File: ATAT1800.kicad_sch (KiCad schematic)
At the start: 336 parts, among them J1 USB_C_Receptacle_USB2.0, SW1 MX_SW_solder, SW10 MX_SW_solder, SW100 MX_SW_solder, SW101 MX_SW_solder, SW102 SW_SPDT, SW11 MX_SW_solder, SW12 MX_SW_solder, SW13 MX_SW_solder, SW14 MX_SW_solder, SW15 MX_SW_solder, SW16 MX_SW_solder, SW17 MX_SW_solder, SW18 MX_SW_solder, SW19 MX_SW_solder, SW2 MX_SW_solder, SW20 MX_SW_solder, SW21 MX_SW_solder, SW22 MX_SW_solder, SW23 MX_SW_solder, SW24 MX_SW_solder, SW25 MX_SW_solder, SW26 MX_SW_solder, SW27 MX_SW_solder, SW28 MX_SW_solder, SW29 MX_SW_solder, SW3 MX_SW_solder, SW30 MX_SW_solder, SW31 MX_SW_solder, SW32 MX_SW_solder, SW33 MX_SW_solder, SW34 MX_SW_solder, SW35 MX_SW_solder, SW36 MX_SW_solder, SW37 MX_SW_solder, SW38 MX_SW_solder, SW39 MX_SW_solder, SW4 MX_SW_solder, SW40 MX_SW_solder, SW41 MX_SW_solder, SW42 MX_SW_solder, SW43 MX_SW_solder, SW44 MX_SW_solder, SW45 MX_SW_solder, SW46 MX_SW_solder, SW47 MX_SW_solder, SW48 MX_SW_solder, SW49 MX_SW_solder, SW5 MX_SW_solder, SW50 MX_SW_solder, SW51 MX_SW_solder, SW52 MX_SW_solder, SW53 MX_SW_solder, SW54 MX_SW_solder, SW55 MX_SW_solder, SW56 MX_SW_solder, SW57 MX_SW_solder, SW58 MX_SW_solder, SW59 MX_SW_solder, SW6 MX_SW_solder, SW60 MX_SW_solder, SW61 MX_SW_solder, SW62 MX_SW_solder, SW63 MX_SW_solder, SW64 MX_SW_solder, SW65 MX_SW_solder, SW66 MX_SW_solder, SW67 MX_SW_solder, SW68 MX_SW_solder, SW69 MX_SW_solder, SW7 MX_SW_solder, SW70 MX_SW_solder, SW71 MX_SW_solder, SW72 MX_SW_solder, SW73 MX_SW_solder, SW74 MX_SW_solder, SW75 MX_SW_solder, SW76 MX_SW_solder, SW77 MX_SW_solder, SW78 MX_SW_solder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

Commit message: update STEP files
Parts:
- R10, R16, R19, R22, R25, R28, R8: value 110k -> 56k
- R11: value 99k -> 51k
- R15: value 77k -> 33k
- R18: value 66k -> 27k
- R21: value 55k -> 22k
- R24: value 44k -> 15k
- R27: value 33k -> 5.6k
- R7: value 88k -> 39k
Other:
- note added: "R_{Iset} = 500/0.010"
- note added: "R_{Iset} = 50kOhm"
- note removed: "R_{Iset} = 110kOhm"
- note removed: "R_{Iset} = 500/0.0045"
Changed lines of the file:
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@@
     (stroke (width 0) (type default))
   )
-  (text "R_{Iset} = 500/0.0045" (at 139.7 278.13 0)
+  (text "R_{Iset} = 500/0.010\n" (at 139.7 278.13 0)
     (effects (font (size 2.54 2.54)) (justify left bottom))
   )
@@
     (effects (font (size 2.54 2.54)) (justify left bottom))
   )
-  (text "R_{Iset} = 110kOhm" (at 139.7 281.94 0)
+  (text "R_{Iset} = 50kOhm" (at 139.7 281.94 0)
     (effects (font (size 2.54 2.54)) (justify left bottom))
   )
@@
       (effects (font (size 1 1)))
     )
-    (property "Value" "88k" (at 118.11 176.53 90)
+    (property "Value" "39k" (at 118.11 176.53 90)
       (effects (font (size 0.8 0.8)))
     )
@@
       (effects (font (size 1 1)))
     )
-    (property "Value" "110k" (at 118.11 231.14 90)
+    (property "Value" "56k" (at 118.11 231.14 90)
       (effects (font (size 0.8 0.8)))
     )
@@
       (effects (font (size 1 1)))
     )
-    (property "Value" "110k" (at 29.21 231.14 90)
+    (property "Value" "56k" (at 29.21 231.14 90)
       (effects (font (size 0.8 0.8)))
     )
@@
       (effects (font (size 1 1)))
     )
-    (property "Value" "77k" (at 207.01 176.53 90)
+    (property "Value" "33k" (at 207.01 176.53 90)
       (effects (font (size 0.8 0.8)))
     )
@@
       (effects (font (size 1 1)))
     )
-    (property "Value" "110k" (at 207.01 284.48 90)
+    (property "Value" "56k" (at 207.01 284.48 90)
       (effects (font (size 0.8 0.8)))
     )
@@
       (effects (font (size 1 1)))
     )
-    (property "Value" "33k" (at 207.01 281.94 90)
+    (property "Value" "5.6k" (at 207.01 281.94 90)
       (effects (font (size 0.8 0.8)))
     )
@@
       (effects (font (size 1 1)))
     )
-    (property "Value" "110k" (at 207.01 231.14 90)
+    (property "Value" "56k" (at 207.01 231.14 90)
       (effects (font (size 0.8 0.8)))
     )
@@
       (effects (font (size 1 1)))
     )
-    (property "Value" "66k" (at 29.21 228.6 90)
+    (property "Value" "27k" (at 29.21 228.6 90)
       (effects (font (size 0.8 0.8)))
     )
@@
       (effects (font (size 1 1)))
     )
-    (property "Value" "110k" (at 207.01 179.07 90)
+    (property "Value" "56k" (at 207.01 179.07 90)
       (effects (font (size 0.8 0.8)))
     )
@@
       (effects (font (size 1 1)))
     )
-    (property "Value" "44k" (at 207.01 228.6 90)
+    (property "Value" "15k" (at 207.01 228.6 90)
       (effects (font (size 0.8 0.8)))
     )
@@
       (effects (font (size 1 1)))
     )
-    (property "Value" "110k" (at 29.21 179.07 90)
+    (property "Value" "56k" (at 29.21 179.07 90)
       (effects (font (size 0.8 0.8)))
     )
@@
       (effects (font (size 1 1)))
     )
-    (property "Value" "110k" (at 118.11 179.07 90)
+    (property "Value" "56k" (at 118.11 179.07 90)
       (effects (font (size 0.8 0.8)))
     )
@@
       (effects (font (size 1 1)))
     )
-    (property "Value" "99k" (at 29.21 176.53 90)
+    (property "Value" "51k" (at 29.21 176.53 90)
       (effects (font (size 0.8 0.8)))
     )
@@
       (effects (font (size 1 1)))
     )
-    (property "Value" "55k" (at 118.11 228.6 90)
+    (property "Value" "22k" (at 118.11 228.6 90)
       (effects (font (size 0.8 0.8)))
     )

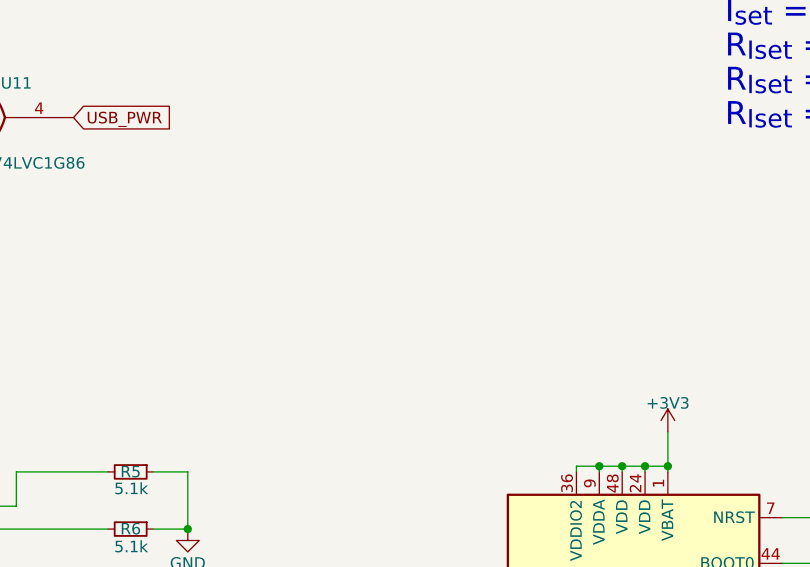
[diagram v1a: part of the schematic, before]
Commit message: add mounting points. fix stab collision
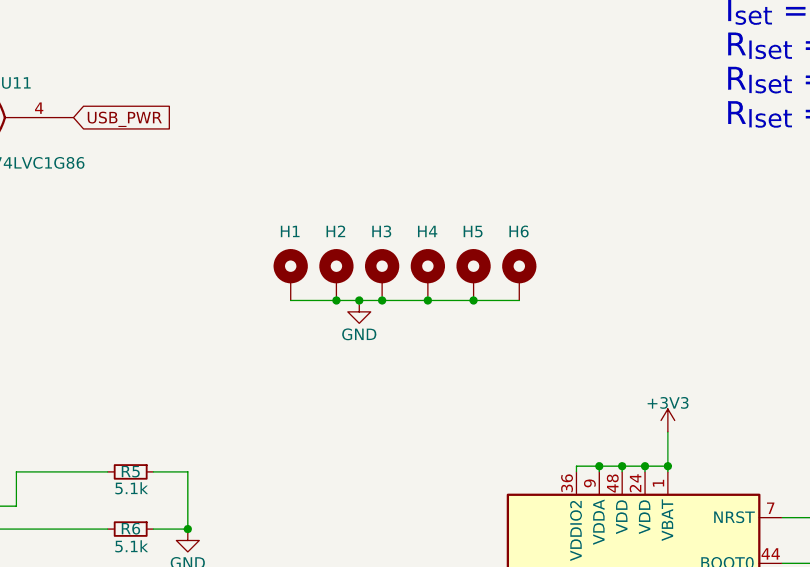
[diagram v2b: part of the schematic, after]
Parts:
- added H1, H2, H3, H4, H5, H6: MountingHole_Pad, MountingHole:MountingHole_3.2mm_M3_Pad_Via, symbol Mechanical:MountingHole_Pad
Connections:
- net GND: now also H1.1, H2.1, H3.1, H4.1, H5.1, H6.1
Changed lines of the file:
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@@
   (junction (at 55.88 46.99) (diameter 0) (color 0 0 0 0)
   )
+  (junction (at 96.52 300.99) (diameter 0) (color 0 0 0 0)
+  )
   (junction (at 25.4 39.37) (diameter 0) (color 0 0 0 0)
   )
+  (junction (at 99.06 300.99) (diameter 0) (color 0 0 0 0)
+  )
   (junction (at 246.38 85.09) (diameter 0) (color 0 0 0 0)
   )
@@
   (junction (at 186.69 158.75) (diameter 0) (color 0 0 0 0)
   )
+  (junction (at 106.68 300.99) (diameter 0) (color 0 0 0 0)
+  )
   (junction (at 97.79 171.45) (diameter 0) (color 0 0 0 0)
   )
@@
   (junction (at 241.3 39.37) (diameter 0) (color 0 0 0 0)
   )
+  (junction (at 111.76 300.99) (diameter 0) (color 0 0 0 0)
+  )
   (junction (at 275.59 274.32) (diameter 0) (color 0 0 0 0)
   )
@@
   (junction (at 157.48 85.09) (diameter 0) (color 0 0 0 0)
   )
+  (junction (at 101.6 300.99) (diameter 0) (color 0 0 0 0)
+  )
   (junction (at 50.8 39.37) (diameter 0) (color 0 0 0 0)
   )
@@
     (stroke (width 0) (type default))
   )
+  (wire (pts (xy 106.68 300.99) (xy 111.76 300.99))
+    (stroke (width 0) (type default))
+  )
   (wire (pts (xy 97.79 228.6) (xy 97.79 231.14))
     (stroke (width 0) (type default))
@@
     (stroke (width 0) (type default))
   )
+  (wire (pts (xy 96.52 300.99) (xy 99.06 300.99))
+    (stroke (width 0) (type default))
+  )
   (wire (pts (xy 97.79 156.21) (xy 97.79 158.75))
     (stroke (width 0) (type default))
@@
     (stroke (width 0) (type default))
   )
+  (wire (pts (xy 99.06 300.99) (xy 101.6 300.99))
+    (stroke (width 0) (type default))
+  )
   (wire (pts (xy 73.66 382.27) (xy 73.66 387.35))
     (stroke (width 0) (type default))
@@
     (stroke (width 0) (type default))
   )
+  (wire (pts (xy 101.6 300.99) (xy 106.68 300.99))
+    (stroke (width 0) (type default))
+  )
   (wire (pts (xy 275.59 297.18) (xy 275.59 299.72))
     (stroke (width 0) (type default))
@@
     (stroke (width 0) (type default))
   )
+  (wire (pts (xy 111.76 300.99) (xy 116.84 300.99))
+    (stroke (width 0) (type default))
+  )
   (wire (pts (xy 19.05 189.23) (xy 19.05 185.42))
     (stroke (width 0) (type default))
@@
     (stroke (width 0) (type default))
   )
+  (wire (pts (xy 91.44 300.99) (xy 96.52 300.99))
+    (stroke (width 0) (type default))
+  )
   (wire (pts (xy 171.45 218.44) (xy 179.07 218.44))
     (stroke (width 0) (type default))
@@
     )
   )
+  (symbol (lib_id "Mechanical:MountingHole_Pad") (at 101.6 298.45 0) (unit 1)
+    (in_bom yes) (on_board yes) (dnp no)
+    (property "Reference" "H3" (at 100.33 293.37 0)
+      (effects (font (size 1.27 1.27)) (justify left))
+    )
+    (property "Value" "MountingHole_Pad" (at 104.14 298.45 0)
+      (effects (font (size 1.27 1.27)) (justify left) hide)
+    )
+    (property "Footprint" "MountingHole:MountingHole_3.2mm_M3_Pad_Via" (at 101.6 298.45 0)
+      (effects (font (size 1.27 1.27)) hide)
+    )
+    (property "Datasheet" "~" (at 101.6 298.45 0)
+      (effects (font (size 1.27 1.27)) hide)
+    )
+    (pin "1")
+    (instances
+      (project "ATAT1800"
+        (path "/649a41cb-a23a-42e1-b0e0-3f26cb53f20e"
+          (reference "H3") (unit 1)
+        )
+      )
+    )
+  )
   (symbol (lib_id "Device:D_Dual_CommonCathode_AAK_Split") (at 170.18 96.52 270) (unit 1)
     (in_bom yes) (on_board yes) (dnp no)
@@
     )
   )
+  (symbol (lib_id "Mechanical:MountingHole_Pad") (at 116.84 298.45 0) (unit 1)
+    (in_bom yes) (on_board yes) (dnp no)
+    (property "Reference" "H6" (at 115.57 293.37 0)
+      (effects (font (size 1.27 1.27)) (justify left))
+    )
+    (property "Value" "MountingHole_Pad" (at 119.38 298.45 0)
+      (effects (font (size 1.27 1.27)) (justify left) hide)
+    )
+    (property "Footprint" "MountingHole:MountingHole_3.2mm_M3_Pad_Via" (at 116.84 298.45 0)
+      (effects (font (size 1.27 1.27)) hide)
+    )
+    (property "Datasheet" "~" (at 116.84 298.45 0)
+      (effects (font (size 1.27 1.27)) hide)
+    )
+    (pin "1")
+    (instances
+      (project "ATAT1800"
+        (path "/649a41cb-a23a-42e1-b0e0-3f26cb53f20e"
+          (reference "H6") (unit 1)
+        )
+      )
+    )
+  )
   (symbol (lib_id "Device:LED") (at 182.88 176.53 0) (mirror x) (unit 1)
     (in_bom yes) (on_board yes) (dnp no)
@@
     )
   )
+  (symbol (lib_id "Mechanical:MountingHole_Pad") (at 91.44 298.45 0) (unit 1)
+    (in_bom yes) (on_board yes) (dnp no)
+    (property "Reference" "H1" (at 90.17 293.37 0)
+      (effects (font (size 1.27 1.27)) (justify left))
+    )
+    (property "Value" "MountingHole_Pad" (at 93.98 298.45 0)
+      (effects (font (size 1.27 1.27)) (justify left) hide)
+    )
+    (property "Footprint" "MountingHole:MountingHole_3.2mm_M3_Pad_Via" (at 91.44 298.45 0)
+      (effects (font (size 1.27 1.27)) hide)
+    )
+    (property "Datasheet" "~" (at 91.44 298.45 0)
+      (effects (font (size 1.27 1.27)) hide)
+    )
+    (pin "1")
+    (instances
+      (project "ATAT1800"
+        (path "/649a41cb-a23a-42e1-b0e0-3f26cb53f20e"
+          (reference "H1") (unit 1)
+        )
+      )
+    )
+  )
   (symbol (lib_id "PCM_marbastlib-mx:MX_SW_solder") (at 243.84 29.21 0) (unit 1)
     (in_bom yes) (on_board yes) (dnp no)
@@
     )
   )
+  (symbol (lib_id "Mechanical:MountingHole_Pad") (at 106.68 298.45 0) (unit 1)
+    (in_bom yes) (on_board yes) (dnp no)
+    (property "Reference" "H4" (at 105.41 293.37 0)
+      (effects (font (size 1.27 1.27)) (justify left))
+    )
+    (property "Value" "MountingHole_Pad" (at 109.22 298.45 0)
+      (effects (font (size 1.27 1.27)) (justify left) hide)
+    )
+    (property "Footprint" "MountingHole:MountingHole_3.2mm_M3_Pad_Via" (at 106.68 298.45 0)
+      (effects (font (size 1.27 1.27)) hide)
+    )
+    (property "Datasheet" "~" (at 106.68 298.45 0)
+      (effects (font (size 1.27 1.27)) hide)
+    )
+    (pin "1")
+    (instances
+      (project "ATAT1800"
+        (path "/649a41cb-a23a-42e1-b0e0-3f26cb53f20e"
+          (reference "H4") (unit 1)
+        )
+      )
+    )
+  )
   (symbol (lib_id "Device:LED") (at 264.16 179.07 0) (mirror x) (unit 1)
     (in_bom yes) (on_board yes) (dnp no)
@@
     )
   )
+  (symbol (lib_id "Mechanical:MountingHole_Pad") (at 96.52 298.45 0) (unit 1)
+    (in_bom yes) (on_board yes) (dnp no)
+    (property "Reference" "H2" (at 95.25 293.37 0)
+      (effects (font (size 1.27 1.27)) (justify left))
+    )
+    (property "Value" "MountingHole_Pad" (at 99.06 298.45 0)
+      (effects (font (size 1.27 1.27)) (justify left) hide)
+    )
+    (property "Footprint" "MountingHole:MountingHole_3.2mm_M3_Pad_Via" (at 96.52 298.45 0)
+      (effects (font (size 1.27 1.27)) hide)
+    )
+    (property "Datasheet" "~" (at 96.52 298.45 0)
+      (effects (font (size 1.27 1.27)) hide)
+    )
+    (pin "1")
+    (instances
+      (project "ATAT1800"
+        (path "/649a41cb-a23a-42e1-b0e0-3f26cb53f20e"
+          (reference "H2") (unit 1)
+        )
+      )
+    )
+  )
   (symbol (lib_id "Device:R_Small") (at 200.66 166.37 90) (unit 1)
     (in_bom yes) (on_board yes) (dnp no)
@@
     )
   )
+  (symbol (lib_id "power:GND") (at 99.06 300.99 0) (unit 1)
+    (in_bom yes) (on_board yes) (dnp no)
+    (property "Reference" "#PWR045" (at 99.06 307.34 0)
+      (effects (font (size 1.27 1.27)) hide)
+    )
+    (property "Value" "GND" (at 99.06 304.8 0)
+      (effects (font (size 1.27 1.27)))
+    )
+    (property "Footprint" "" (at 99.06 300.99 0)
+      (effects (font (size 1.27 1.27)) hide)
+    )
+    (property "Datasheet" "" (at 99.06 300.99 0)
+      (effects (font (size 1.27 1.27)) hide)
+    )
+    (pin "1")
+    (instances
+      (project "ATAT1800"
+        (path "/649a41cb-a23a-42e1-b0e0-3f26cb53f20e"
+          (reference "#PWR045") (unit 1)
+        )
+      )
+      (project "board_arm"
+        (path "/d69fdd30-26b7-4d0b-9202-06d7a8c54869"
+          (reference "#PWR0114") (unit 1)
+        )
+      )
+    )
+  )
   (symbol (lib_id "Device:LED") (at 182.88 171.45 0) (mirror x) (unit 1)
     (in_bom yes) (on_board yes) (dnp no)
@@
         )
       )
+    )
+  )
+  (symbol (lib_id "Mechanical:MountingHole_Pad") (at 111.76 298.45 0) (unit 1)
+    (in_bom yes) (on_board yes) (dnp no)
+    (property "Reference" "H5" (at 110.49 293.37 0)
+      (effects (font (size 1.27 1.27)) (justify left))
+    )
+    (property "Value" "MountingHole_Pad" (at 114.3 298.45 0)
+      (effects (font (size 1.27 1.27)) (justify left) hide)
+    )
+    (property "Footprint" "MountingHole:MountingHole_3.2mm_M3_Pad_Via" (at 111.76 298.45 0)
+      (effects (font (size 1.27 1.27)) hide)
+    )
+    (property "Datasheet" "~" (at 111.76 298.45 0)
+      (effects (font (size 1.27 1.27)) hide)
+    )
+    (pin "1")
+    (instances
+      (project "ATAT1800"
+        (path "/649a41cb-a23a-42e1-b0e0-3f26cb53f20e"
+          (reference "H5") (unit 1)
+        )
+      )

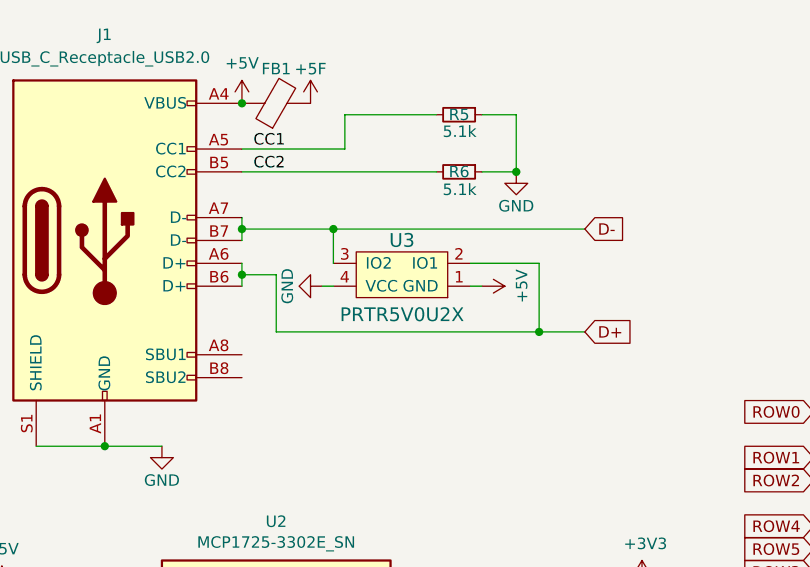
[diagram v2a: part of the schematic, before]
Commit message: fix input diode
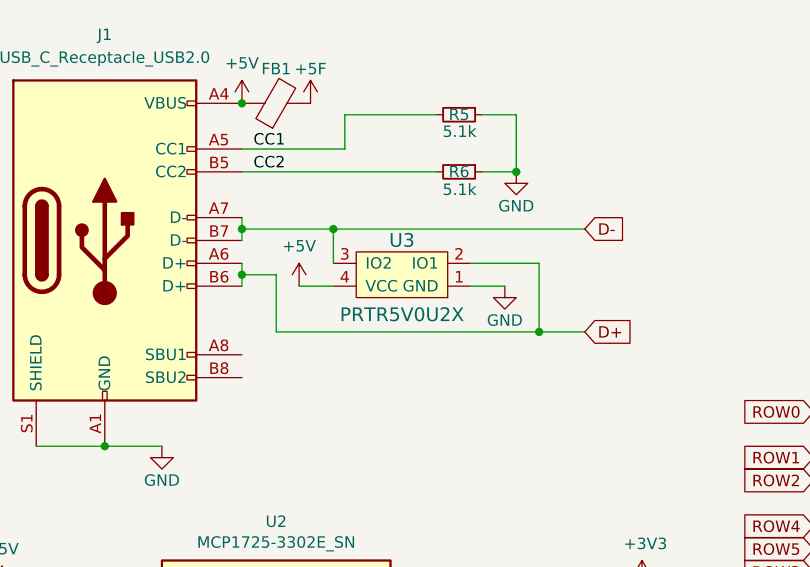
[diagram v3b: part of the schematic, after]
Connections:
- net +5V: now also U3.4 (VCC); no longer U3.1 (GND)
- net GND: now also U3.1 (GND); no longer U3.4 (VCC)
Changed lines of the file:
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@@
     (stroke (width 0) (type default))
   )
+  (wire (pts (xy 74.93 339.09) (xy 78.74 339.09))
+    (stroke (width 0) (type default))
+  )
   (wire (pts (xy 25.4 64.77) (xy 25.4 77.47))
     (stroke (width 0) (type default))
@@
     (stroke (width 0) (type default))
   )
-  (wire (pts (xy 59.69 339.09) (xy 58.42 339.09))
-    (stroke (width 0) (type default))
-  )
   (wire (pts (xy 186.69 231.14) (xy 186.69 233.68))
     (stroke (width 0) (type default))
@@
     (stroke (width 0) (type default))
   )
+  (wire (pts (xy 55.88 339.09) (xy 59.69 339.09))
+    (stroke (width 0) (type default))
+  )
   (wire (pts (xy 125.73 320.04) (xy 125.73 319.405))
     (stroke (width 0) (type default))
@@
     (stroke (width 0) (type default))
   )
-  (wire (pts (xy 76.2 339.09) (xy 74.93 339.09))
-    (stroke (width 0) (type default))
-  )
   (wire (pts (xy 114.3 77.47) (xy 114.3 107.95))
     (stroke (width 0) (type default))
@@
     )
   )
-  (symbol (lib_id "power:+5V") (at 76.2 339.09 270) (mirror x) (unit 1)
+  (symbol (lib_id "power:+5V") (at 55.88 339.09 0) (mirror y) (unit 1)
     (in_bom yes) (on_board yes) (dnp no)
-    (property "Reference" "#PWR09" (at 72.39 339.09 0)
+    (property "Reference" "#PWR09" (at 55.88 342.9 0)
       (effects (font (size 1.27 1.27)) hide)
     )
-    (property "Value" "+5V" (at 80.645 339.09 0)
+    (property "Value" "+5V" (at 55.88 334.645 0)
       (effects (font (size 1.27 1.27)))
     )
-    (property "Footprint" "" (at 76.2 339.09 0)
+    (property "Footprint" "" (at 55.88 339.09 0)
       (effects (font (size 1.27 1.27)) hide)
     )
-    (property "Datasheet" "" (at 76.2 339.09 0)
+    (property "Datasheet" "" (at 55.88 339.09 0)
       (effects (font (size 1.27 1.27)) hide)
     )
@@
     )
   )
-  (symbol (lib_id "power:GND") (at 58.42 339.09 270) (mirror x) (unit 1)
+  (symbol (lib_id "power:GND") (at 78.74 339.09 0) (unit 1)
     (in_bom yes) (on_board yes) (dnp no)
-    (property "Reference" "#PWR015" (at 52.07 339.09 0)
+    (property "Reference" "#PWR015" (at 78.74 345.44 0)
       (effects (font (size 1.27 1.27)) hide)
     )
-    (property "Value" "GND" (at 54.61 339.09 0)
+    (property "Value" "GND" (at 78.74 342.9 0)
       (effects (font (size 1.27 1.27)))
     )
-    (property "Footprint" "" (at 58.42 339.09 0)
+    (property "Footprint" "" (at 78.74 339.09 0)
       (effects (font (size 1.27 1.27)) hide)
     )
-    (property "Datasheet" "" (at 58.42 339.09 0)
+    (property "Datasheet" "" (at 78.74 339.09 0)
       (effects (font (size 1.27 1.27)) hide)
     )

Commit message: upgrade files to V9
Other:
- note added: "Address 0x31"
- note added: "Address 0x33"
- note added: "Address 0x34"
- note added: "Address 0x35"
- note added: "Address 0x36"
- note added: "Address 0x37"
- note added: "Address 0x39"
